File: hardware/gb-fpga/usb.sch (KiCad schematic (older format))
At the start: 2 parts, among them J1 USB_B_Micro, U3 FT2232HQ

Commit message: Replace micro usb with usb type c connector
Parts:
- removed J1: USB_B_Micro, Connector_USB:USB_Micro-B_Amphenol_10103594-0001LF_Horizontal, symbol Connector:USB_B_Micro
- added J1: USB_C_Receptacle_USB2.0, Connector_USB:USB_C_Receptacle_XKB_U262-16XN-4BVC11, symbol Connector:USB_C_Receptacle_USB2.0
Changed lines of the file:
@@
 $Descr A4 11693 8268
 encoding utf-8
-Sheet 5 6
+Sheet 4 6
 Title "USB"
 Date ""
@@
 F 3 "https://www.ftdichip.com/Support/Documents/DataSheets/ICs/DS_FT2232H.pdf" H 5850 3800 50  0001 C CNN
 	1    5850 3800
-	1    0    0    -1
-$EndComp
-$Comp
-L Connector:USB_B_Micro J1
-U 1 1 60D33076
-P 3000 3700
-F 0 "J1" H 3057 4167 50  0000 C CNN
-F 1 "USB_B_Micro" H 3057 4076 50  0000 C CNN
-F 2 "Connector_USB:USB_Micro-B_Amphenol_10103594-0001LF_Horizontal" H 3150 3650 50  0001 C CNN
-F 3 "~" H 3150 3650 50  0001 C CNN
-	1    3000 3700
-	1    0    0    -1
-$EndComp
-$Comp
-L power:GND #PWR0103
-U 1 1 60D34652
-P 3000 4100
-F 0 "#PWR0103" H 3000 3850 50  0001 C CNN
-F 1 "GND" H 3005 3927 50  0000 C CNN
-F 2 "" H 3000 4100 50  0001 C CNN
-F 3 "" H 3000 4100 50  0001 C CNN
-	1    3000 4100
 	1    0    0    -1
 $EndComp
@@
 $EndComp
 Connection ~ 6250 6150
+$Comp
+L Connector:USB_C_Receptacle_USB2.0 J1
+U 1 1 60E1E155
+P 1650 4100
+F 0 "J1" H 1757 4967 50  0000 C CNN
+F 1 "USB_C_Receptacle_USB2.0" H 1757 4876 50  0000 C CNN
+F 2 "Connector_USB:USB_C_Receptacle_XKB_U262-16XN-4BVC11" H 1800 4100 50  0001 C CNN
+F 3 "https://www.usb.org/sites/default/files/documents/usb_type-c.zip" H 1800 4100 50  0001 C CNN
+	1    1650 4100
+	1    0    0    -1
+$EndComp
 $EndSCHEMATC

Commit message: Add USB connections
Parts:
- added R10, R11, R12, R13: 10k, Resistor_SMD:R_0603_1608Metric, symbol Device:R_Small
- added R14: 12k, Resistor_SMD:R_0603_1608Metric, symbol Device:R_Small
- added R15: 1k, Resistor_SMD:R_0603_1608Metric, symbol Device:R_Small
- added R16, R17: 4.7k, Resistor_SMD:R_0603_1608Metric, symbol Device:R_Small
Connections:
- net GND: now also J1.A1 (GND), J1.A12 (GND), J1.B1 (GND), J1.B12 (GND), J1.S1 (SHIELD), U3.10 (AGND), U3.13 (TEST), R14.2, R16.2, R17.2
- net at U3.14 (~RESET): now also R15.1
- net TCK: now reaches U3.16 (ADBUS0)
- net TCK: now also R13.2
- net TDI: now reaches U3.17 (ADBUS1)
- net TDI: now also R12.2
- net TDO: now reaches U3.18 (ADBUS2)
- net TDO: now also R11.2
- net TMS: now reaches U3.19 (ADBUS3)
- net TMS: now also R10.2
- net TX: now reaches U3.38 (BDBUS0)
- net RX: now reaches U3.39 (BDBUS1)
- net at U3.6 (REF): now also R14.1
- net at U3.7 (DM): now also J1.A7 (D-), J1.B7 (D-)
- net at U3.8 (DP): now also J1.A6 (D+), J1.B6 (D+)
- net at J1.A5 (CC1): now also R17.1
- net at J1.B5 (CC2): now also R16.1
- new net +3V3: R10.1, R11.1, R12.1, R13.1, R15.2
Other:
- moved on the sheet: J1

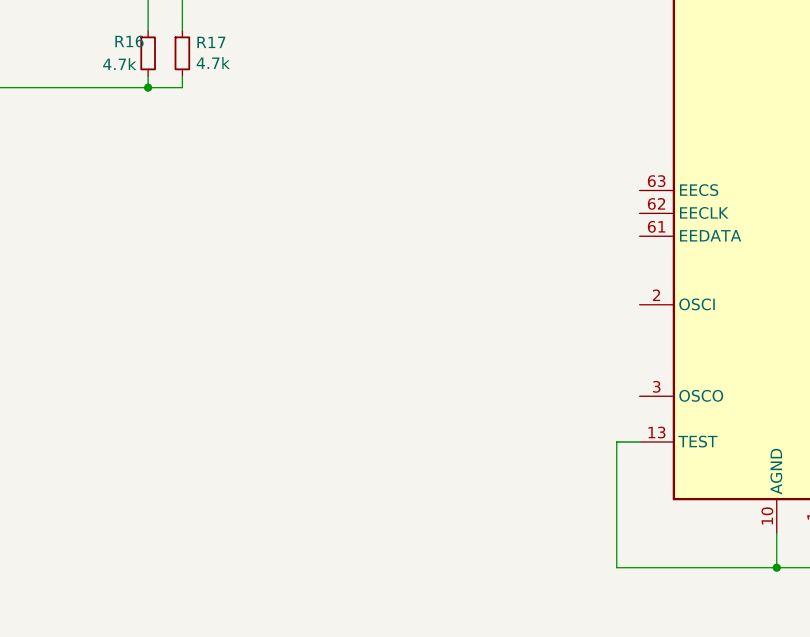
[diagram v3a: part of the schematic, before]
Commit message: Add oscillator
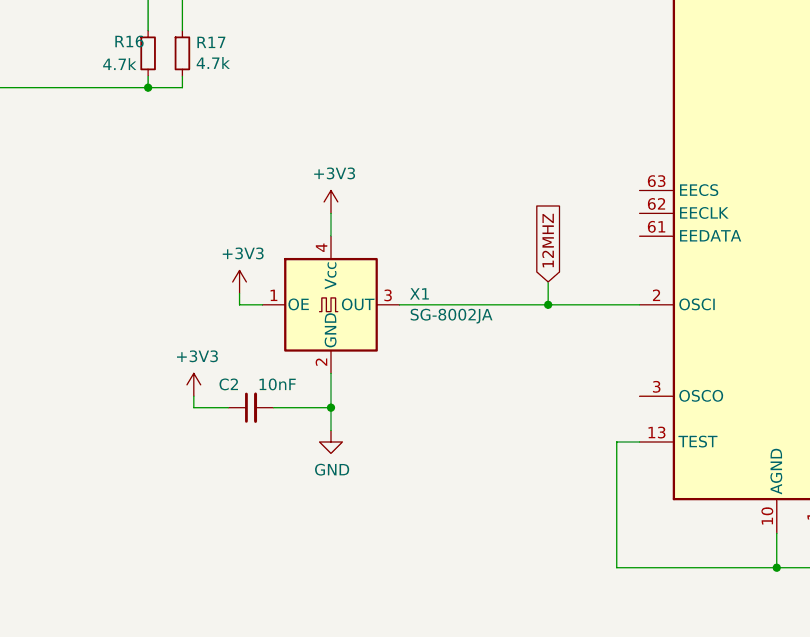
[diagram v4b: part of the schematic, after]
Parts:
- added C2: 10nF, Capacitor_SMD:C_0603_1608Metric, symbol Device:C_Small
- added X1: SG-8002JA, Oscillator:Oscillator_SMD_Abracon_ASE-4Pin_3.2x2.5mm, symbol Oscillator:SG-8002JA
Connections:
- net +3V3: now also C2.1, X1.1 (OE), X1.4 (Vcc)
- net GND: now also C2.2, X1.2 (GND)
- net 12MHZ: now reaches U3.2 (OSCI)
- net 12MHZ: now also X1.3 (OUT)
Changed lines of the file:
@@
 Text GLabel 8050 3800 2    50   Input ~ 0
 RX
+$Comp
+L Oscillator:SG-8002JA X1
+U 1 1 60ECBD8E
+P 3300 5000
+F 0 "X1" H 3644 5046 50  0000 L CNN
+F 1 "SG-8002JA" H 3644 4955 50  0000 L CNN
+F 2 "Oscillator:Oscillator_SMD_Abracon_ASE-4Pin_3.2x2.5mm" H 4000 4650 50  0001 C CNN
+F 3 "https://support.epson.biz/td/api/doc_check.php?mode=dl&lang=en&Parts=SG-8002DC" H 3200 5000 50  0001 C CNN
+	1    3300 5000
+	1    0    0    -1
+$EndComp
+Wire Wire Line
+	3600 5000 4250 5000
+$Comp
+L Device:C_Small C2
+U 1 1 60ECE62B
+P 2950 5450
+F 0 "C2" V 3050 5500 50  0000 L CNN
+F 1 "10nF" V 3050 5250 50  0000 L CNN
+F 2 "Capacitor_SMD:C_0603_1608Metric" H 2950 5450 50  0001 C CNN
+F 3 "~" H 2950 5450 50  0001 C CNN
+	1    2950 5450
+	0    -1   -1   0
+$EndComp
+Wire Wire Line
+	3050 5450 3300 5450
+Wire Wire Line
+	3300 5450 3300 5300
+$Comp
+L power:GND #PWR0133
+U 1 1 60ED319C
+P 3300 5550
+F 0 "#PWR0133" H 3300 5300 50  0001 C CNN
+F 1 "GND" H 3305 5377 50  0000 C CNN
+F 2 "" H 3300 5550 50  0001 C CNN
+F 3 "" H 3300 5550 50  0001 C CNN
+	1    3300 5550
+	1    0    0    -1
+$EndComp
+Wire Wire Line
+	3300 5550 3300 5450
+Connection ~ 3300 5450
+Wire Wire Line
+	3300 4600 3300 4700
+$Comp
+L power:+3V3 #PWR0134
+U 1 1 60ED4C57
+P 3300 4600
+F 0 "#PWR0134" H 3300 4450 50  0001 C CNN
+F 1 "+3V3" H 3315 4773 50  0000 C CNN
+F 2 "" H 3300 4600 50  0001 C CNN
+F 3 "" H 3300 4600 50  0001 C CNN
+	1    3300 4600
+	1    0    0    -1
+$EndComp
+$Comp
+L power:+3V3 #PWR0135
+U 1 1 60ED7EA6
+P 2900 4950
+F 0 "#PWR0135" H 2900 4800 50  0001 C CNN
+F 1 "+3V3" H 2915 5123 50  0000 C CNN
+F 2 "" H 2900 4950 50  0001 C CNN
+F 3 "" H 2900 4950 50  0001 C CNN
+	1    2900 4950
+	1    0    0    -1
+$EndComp
+$Comp
+L power:+3V3 #PWR0136
+U 1 1 60ED878B
+P 2700 5400
+F 0 "#PWR0136" H 2700 5250 50  0001 C CNN
+F 1 "+3V3" H 2715 5573 50  0000 C CNN
+F 2 "" H 2700 5400 50  0001 C CNN
+F 3 "" H 2700 5400 50  0001 C CNN
+	1    2700 5400
+	1    0    0    -1
+$EndComp
+Wire Wire Line
+	2700 5400 2700 5450
+Wire Wire Line
+	2700 5450 2850 5450
+Wire Wire Line
+	2900 4950 2900 5000
+Wire Wire Line
+	2900 5000 3000 5000
+Text GLabel 4250 4900 1    50   Input ~ 0
+12MHZ
+Wire Wire Line
+	4250 4900 4250 5000
+Connection ~ 4250 5000
+Wire Wire Line
+	4250 5000 4650 5000
 $EndSCHEMATC

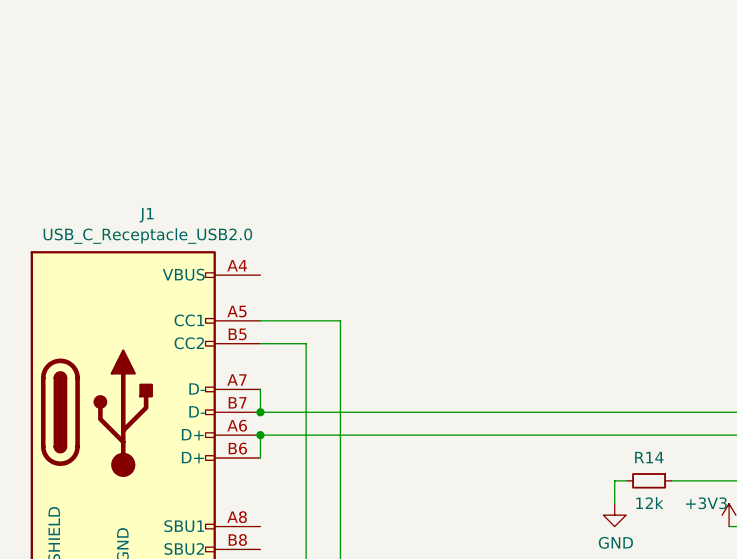
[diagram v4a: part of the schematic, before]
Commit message: Add LTC3555
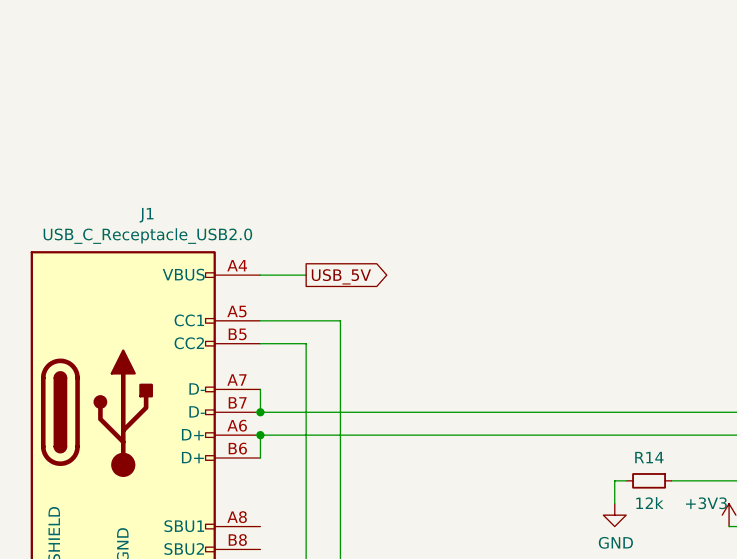
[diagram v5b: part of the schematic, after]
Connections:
- net USB_5V: now reaches J1.A4 (VBUS), J1.A9 (VBUS), J1.B4 (VBUS), J1.B9 (VBUS)
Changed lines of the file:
@@
 $Descr A4 11693 8268
 encoding utf-8
-Sheet 4 6
+Sheet 4 7
 Title "USB"
 Date ""
@@
 Wire Wire Line
 	4250 5000 4650 5000
+Wire Wire Line
+	2500 2300 2300 2300
+Text GLabel 2500 2300 2    50   Output ~ 0
+USB_5V
 $EndSCHEMATC

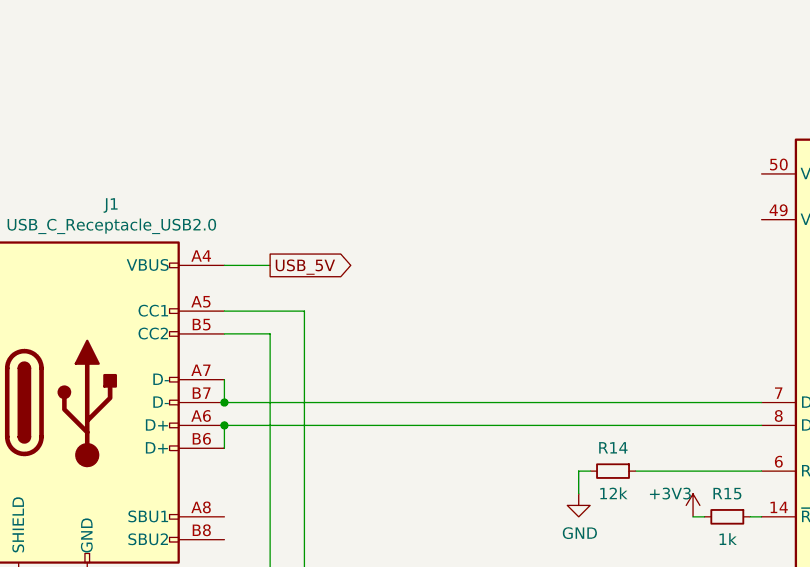
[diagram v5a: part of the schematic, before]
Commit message: Add reverse polarity protection to usb
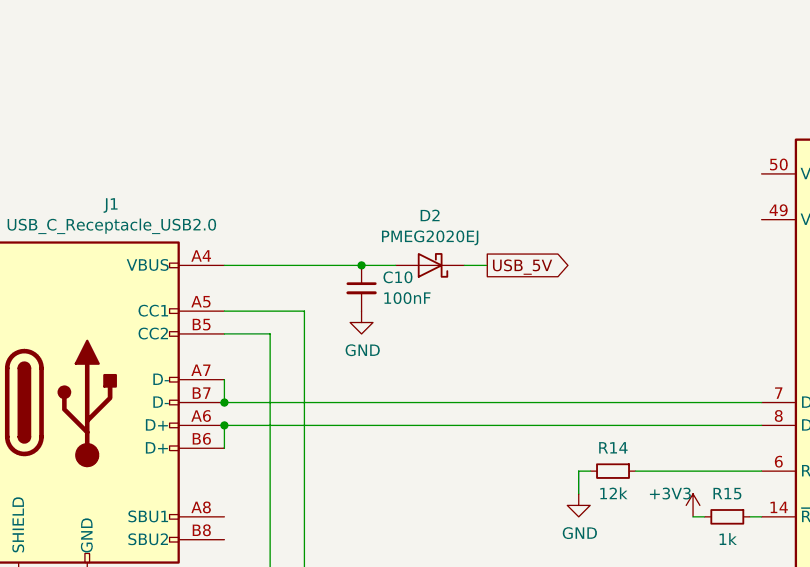
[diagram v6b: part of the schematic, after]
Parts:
- added C10: 100nF, Capacitor_SMD:C_0603_1608Metric, symbol Device:C_Small
- added D2: PMEG2020EJ, Diode_SMD:D_SOD-323F, symbol Diode:PMEG2020EJ
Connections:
- net GND: now also C10.2
- net USB_5V: now also D2.1 (K); no longer J1.A4 (VBUS), J1.A9 (VBUS), J1.B4 (VBUS), J1.B9 (VBUS)
- new net: C10.1, D2.2 (A), J1.A4 (VBUS), J1.A9 (VBUS), J1.B4 (VBUS), J1.B9 (VBUS)
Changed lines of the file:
@@
 	4250 5000 4650 5000
 Wire Wire Line
-	2500 2300 2300 2300
-Text GLabel 2500 2300 2    50   Output ~ 0
+	2900 2300 2300 2300
+Text GLabel 3450 2300 2    50   Output ~ 0
 USB_5V
+$Comp
+L Diode:PMEG2020EJ D2
+U 1 1 60DEA6C7
+P 3200 2300
+F 0 "D2" H 3200 2084 50  0000 C CNN
+F 1 "PMEG2020EJ" H 3200 2175 50  0000 C CNN
+F 2 "Diode_SMD:D_SOD-323F" H 3200 2125 50  0001 C CNN
+F 3 "https://assets.nexperia.com/documents/data-sheet/PMEG2020EH_EJ.pdf" H 3200 2300 50  0001 C CNN
+	1    3200 2300
+	-1   0    0    1
+$EndComp
+Wire Wire Line
+	3350 2300 3450 2300
+$Comp
+L Device:C_Small C10
+U 1 1 60DF265C
+P 2900 2400
+F 0 "C10" H 2992 2446 50  0000 L CNN
+F 1 "100nF" H 2992 2355 50  0000 L CNN
+F 2 "Capacitor_SMD:C_0603_1608Metric" H 2900 2400 50  0001 C CNN
+F 3 "~" H 2900 2400 50  0001 C CNN
+	1    2900 2400
+	1    0    0    -1
+$EndComp
+Wire Wire Line
+	2900 2300 3050 2300
+Connection ~ 2900 2300
+$Comp
+L power:GND #PWR0150
+U 1 1 60DF6310
+P 2900 2500
+F 0 "#PWR0150" H 2900 2250 50  0001 C CNN
+F 1 "GND" H 2905 2327 50  0000 C CNN
+F 2 "" H 2900 2500 50  0001 C CNN
+F 3 "" H 2900 2500 50  0001 C CNN
+	1    2900 2500
+	1    0    0    -1
+$EndComp
 $EndSCHEMATC

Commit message: Switch from 0603 to 0402 footprints
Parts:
- C10, C2: footprint Capacitor_SMD:C_0603_1608Metric -> Capacitor_SMD:C_0402_1005Metric
- R10, R11, R12, R13, R14, R15, R16, R17: footprint Resistor_SMD:R_0603_1608Metric -> Resistor_SMD:R_0402_1005Metric
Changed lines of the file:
@@
 F 0 "R17" H 2709 3946 50  0000 L CNN
 F 1 "4.7k" H 2709 3855 50  0000 L CNN
-F 2 "Resistor_SMD:R_0603_1608Metric" H 2650 3900 50  0001 C CNN
+F 2 "Resistor_SMD:R_0402_1005Metric" H 2650 3900 50  0001 C CNN
 F 3 "~" H 2650 3900 50  0001 C CNN
 	1    2650 3900
@@
 F 0 "R16" H 2350 3950 50  0000 L CNN
 F 1 "4.7k" H 2300 3850 50  0000 L CNN
-F 2 "Resistor_SMD:R_0603_1608Metric" H 2500 3900 50  0001 C CNN
+F 2 "Resistor_SMD:R_0402_1005Metric" H 2500 3900 50  0001 C CNN
 F 3 "~" H 2500 3900 50  0001 C CNN
 	1    2500 3900
@@
 F 0 "R14" V 3900 3200 50  0000 C CNN
 F 1 "12k" V 4100 3200 50  0000 C CNN
-F 2 "Resistor_SMD:R_0603_1608Metric" H 4000 3200 50  0001 C CNN
+F 2 "Resistor_SMD:R_0402_1005Metric" H 4000 3200 50  0001 C CNN
 F 3 "~" H 4000 3200 50  0001 C CNN
 	1    4000 3200
@@
 F 0 "R15" V 4400 3400 50  0000 C CNN
 F 1 "1k" V 4600 3400 50  0000 C CNN
-F 2 "Resistor_SMD:R_0603_1608Metric" H 4500 3400 50  0001 C CNN
+F 2 "Resistor_SMD:R_0402_1005Metric" H 4500 3400 50  0001 C CNN
 F 3 "~" H 4500 3400 50  0001 C CNN
 	1    4500 3400
@@
 F 0 "R10" H 7259 1646 50  0000 L CNN
 F 1 "10k" H 7259 1555 50  0000 L CNN
-F 2 "Resistor_SMD:R_0603_1608Metric" H 7200 1600 50  0001 C CNN
+F 2 "Resistor_SMD:R_0402_1005Metric" H 7200 1600 50  0001 C CNN
 F 3 "~" H 7200 1600 50  0001 C CNN
 	1    7200 1600
@@
 F 0 "R11" H 7509 1646 50  0000 L CNN
 F 1 "10k" H 7509 1555 50  0000 L CNN
-F 2 "Resistor_SMD:R_0603_1608Metric" H 7450 1600 50  0001 C CNN
+F 2 "Resistor_SMD:R_0402_1005Metric" H 7450 1600 50  0001 C CNN
 F 3 "~" H 7450 1600 50  0001 C CNN
 	1    7450 1600
@@
 F 0 "R12" H 7759 1646 50  0000 L CNN
 F 1 "10k" H 7759 1555 50  0000 L CNN
-F 2 "Resistor_SMD:R_0603_1608Metric" H 7700 1600 50  0001 C CNN
+F 2 "Resistor_SMD:R_0402_1005Metric" H 7700 1600 50  0001 C CNN
 F 3 "~" H 7700 1600 50  0001 C CNN
 	1    7700 1600
@@
 F 0 "R13" H 8009 1646 50  0000 L CNN
 F 1 "10k" H 8009 1555 50  0000 L CNN
-F 2 "Resistor_SMD:R_0603_1608Metric" H 7950 1600 50  0001 C CNN
+F 2 "Resistor_SMD:R_0402_1005Metric" H 7950 1600 50  0001 C CNN
 F 3 "~" H 7950 1600 50  0001 C CNN
 	1    7950 1600
@@
 F 0 "C2" V 3050 5500 50  0000 L CNN
 F 1 "10nF" V 3050 5250 50  0000 L CNN
-F 2 "Capacitor_SMD:C_0603_1608Metric" H 2950 5450 50  0001 C CNN
+F 2 "Capacitor_SMD:C_0402_1005Metric" H 2950 5450 50  0001 C CNN
 F 3 "~" H 2950 5450 50  0001 C CNN
 	1    2950 5450
@@
 F 0 "C10" H 2992 2446 50  0000 L CNN
 F 1 "100nF" H 2992 2355 50  0000 L CNN
-F 2 "Capacitor_SMD:C_0603_1608Metric" H 2900 2400 50  0001 C CNN
+F 2 "Capacitor_SMD:C_0402_1005Metric" H 2900 2400 50  0001 C CNN
 F 3 "~" H 2900 2400 50  0001 C CNN
 	1    2900 2400
